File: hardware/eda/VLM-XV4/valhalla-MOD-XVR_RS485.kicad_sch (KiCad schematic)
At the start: 22 parts, among them J1 ModBUS, J2 BUS, U1 MAX3483, U2 ISO1410, U3 74LS06, U4 L78L33_TO92

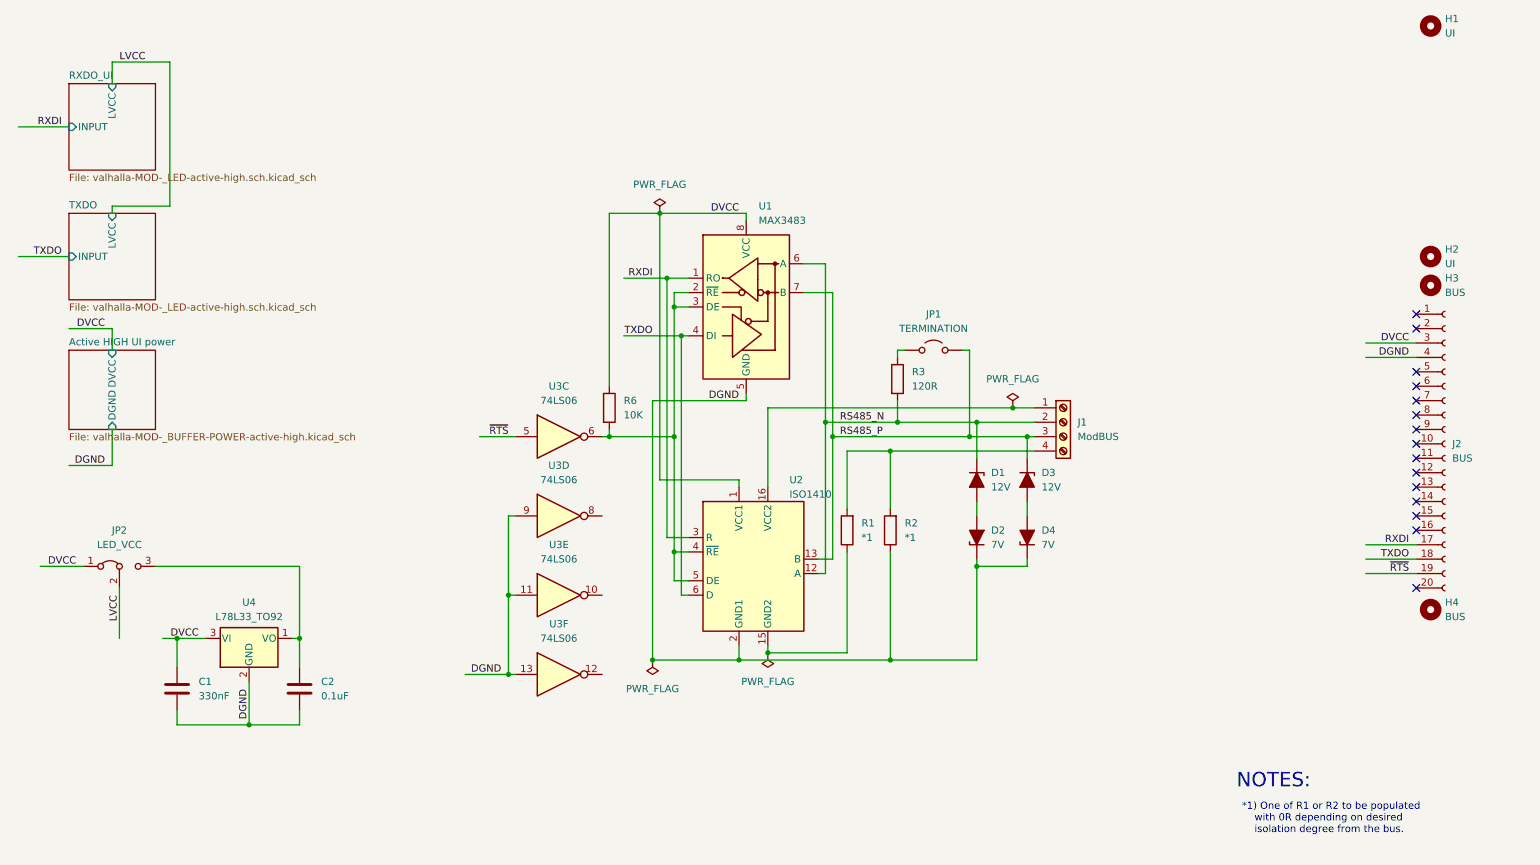
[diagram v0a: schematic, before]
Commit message: UPDATE: finalized schematic of XVR(RS485)
  - found a solution for Vio transparency using a buck-boost regulator
    module, this in turn opened the way to cheap 5V-powered RS485
    transceivers.
  - done initial component placement on the PCB, routing to follow.
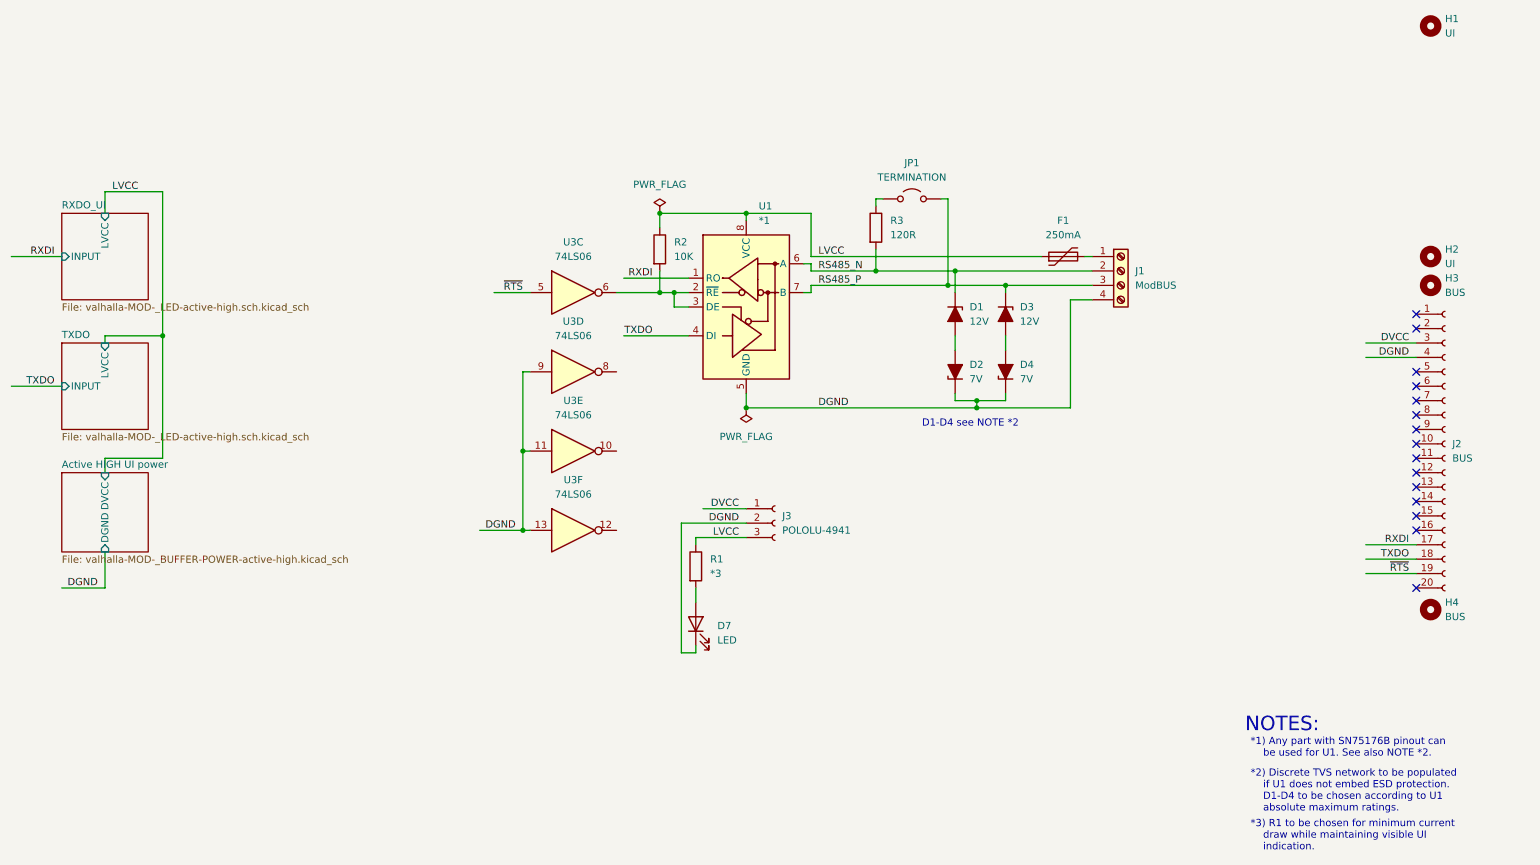
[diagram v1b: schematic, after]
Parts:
- removed C1: 330nF, Capacitor_THT:C_Rect_L4.6mm_W2.0mm_P2.50mm_MKS02_FKP02, symbol Device:C
- removed C2: 0.1uF, Capacitor_THT:C_Rect_L4.6mm_W2.0mm_P2.50mm_MKS02_FKP02, symbol Device:C
- removed JP2: LED_VCC, Connector_PinHeader_2.54mm:PinHeader_1x03_P2.54mm_Vertical, symbol Jumper:Jumper_3_Bridged12
- removed R2: *1, Resistor_SMD:R_1206_3216Metric, symbol Device:R
- removed U2: ISO1410, Package_SO:SOIC-16W_7.5x10.3mm_P1.27mm, symbol valhalla-collected:ISO1410
- removed U4: L78L33_TO92, Package_TO_SOT_THT:TO-92_Wide, symbol Regulator_Linear:L78L33_TO92
- added D7: LED, LED_THT:LED_D3.0mm_Horizontal_O1.27mm_Z2.0mm, symbol Device:LED
- added F1: 250mA, Capacitor_THT:C_Disc_D7.5mm_W4.4mm_P5.00mm, symbol Device:Polyfuse
- added J3: POLOLU-4941, Connector_PinSocket_2.54mm:PinSocket_1x03_P2.54mm_Horizontal, symbol Connector:Conn_01x03_Socket
- D1, D2, D3, D4: footprint (none) -> Diode_THT:D_DO-41_SOD81_P10.16mm_Horizontal
- JP1: footprint (none) -> Connector_PinHeader_2.54mm:PinHeader_1x02_P2.54mm_Vertical
- R1: value *1 -> *3; footprint Resistor_SMD:R_1206_3216Metric -> Resistor_THT:R_Axial_DIN0207_L6.3mm_D2.5mm_P5.08mm_Vertical
- R2: renamed from R6; footprint (none) -> Resistor_THT:R_Axial_DIN0207_L6.3mm_D2.5mm_P5.08mm_Vertical
- R3: footprint (none) -> Resistor_THT:R_Axial_DIN0207_L6.3mm_D2.5mm_P5.08mm_Vertical
- U1: value MAX3483 -> *1; footprint Package_SO:SOIC-8_3.9x4.9mm_P1.27mm -> Package_DIP:DIP-8_W7.62mm
- U3: footprint (none) -> Package_DIP:DIP-14_W7.62mm
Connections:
- net DGND: now also J1.4 (Pin_4), D7.1 (K), J3.2 (Pin_2)
- net DVCC: now also J3.1 (Pin_1); no longer R2.1, U1.8 (VCC)
- net LVCC: now also R1.1, R2.1, U1.8 (VCC), F1.1, J3.3 (Pin_3)
- net at R1.2: now also D7.2 (A); no longer J1.4 (Pin_4)
- net at J1.1 (Pin_1): now also F1.2
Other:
- note added: "*1) Any part with SN75176B pinout can be used for U1. See also NOTE *2."
- note added: "*2) Discrete TVS network to be populated if U1 does not embed ESD protection. D1-D4 to be chosen according to U1 absolute maximum ratings."
- note added: "*3) R1 to be chosen for minimum current draw while maintaining visible UI indication."
- note added: "D1-D4 see NOTE *2"
- note removed: "*1) One of R1 or R2 to be populated with 0R depending on desired isolation degree from the bus."
- moved on the sheet: D1, D2, D3, D4, J1, JP1, R2, R3, U3C, U3D, U3E, U3F

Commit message: UPDATE: XVR(RS485) RTM and XVR(RS232) started
  - after the final cosmetic tweaks, XVR(RS485) has reached RTM status
  - started work on XVR(RS232), schematic is mostly done -- save for
    the UI.
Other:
- moved on the sheet: F1
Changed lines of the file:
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@@
 	(wire
 		(pts
-			(xy 163.83 58.42) (xy 204.47 58.42)
+			(xy 163.83 58.42) (xy 195.58 58.42)
 		)
 		(stroke
@@
 	(wire
 		(pts
-			(xy 212.09 58.42) (xy 213.36 58.42)
+			(xy 203.2 58.42) (xy 213.36 58.42)
 		)
 		(stroke
@@
 		(property "Netclass" "DCD_Power"
 			(at 140.3985 48.26 0)
+			(effects
+				(font
+					(size 1.27 1.27)
+					(italic yes)
+				)
+				(justify left)
+			)
+		)
+	)
+	(netclass_flag ""
+		(length 2.54)
+		(shape round)
+		(at 212.09 58.42 0)
+		(fields_autoplaced yes)
+		(effects
+			(font
+				(size 1.27 1.27)
+			)
+			(justify left bottom)
+		)
+		(property "Netclass" "DCD_Power"
+			(at 212.7885 55.88 0)
 			(effects
 				(font
@@
 	(symbol
 		(lib_id "Device:Polyfuse")
-		(at 208.28 58.42 90)
+		(at 199.39 58.42 90)
 		(unit 1)
 		(exclude_from_sim no)
@@
 		(fields_autoplaced yes)
 		(property "Reference" "F1"
-			(at 208.28 52.07 90)
+			(at 199.39 52.07 90)
 			(effects
 				(font
@@
 		)
 		(property "Value" "250mA"
-			(at 208.28 54.61 90)
+			(at 199.39 54.61 90)
 			(effects
 				(font
@@
 		)
 		(property "Footprint" "Capacitor_THT:C_Disc_D7.5mm_W4.4mm_P5.00mm"
-			(at 213.36 57.15 0)
+			(at 204.47 57.15 0)
 			(effects
 				(font
@@
 		)
 		(property "Datasheet" "~"
-			(at 208.28 58.42 0)
+			(at 199.39 58.42 0)
 			(effects
 				(font
@@
 		)
 		(property "Description" "Resettable fuse, polymeric positive temperature coefficient"
-			(at 208.28 58.42 0)
-			(effects
-				(font
+			(at 199.39 58.42 0)
+			(effects
+				(font

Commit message: UPDATE: updated MOD-XVR(RS485) to the latest specification.
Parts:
- removed D7: LED, LED_THT:LED_D3.0mm_Horizontal_O1.27mm_Z2.0mm, symbol Device:LED
- removed J3: POLOLU-4941, Connector_PinSocket_2.54mm:PinSocket_1x03_P2.54mm_Horizontal, symbol Connector:Conn_01x03_Socket
- removed R1: *3, Resistor_THT:R_Axial_DIN0207_L6.3mm_D2.5mm_P5.08mm_Vertical, symbol Device:R
- added D5, D6: R, LED_THT:LED_D3.0mm_Horizontal_O1.27mm_Z2.0mm, symbol Device:LED
- added R4, R5: *3, Resistor_THT:R_Axial_DIN0207_L6.3mm_D2.5mm_P5.08mm_Vertical, symbol Device:R
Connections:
- net DGND: now also J2.6 (Pin_6), U3.7 (GND)
- net DVCC: now also F1.1, R2.1, U1.8 (VCC), U3.14 (VCC)
- net LVCC: now also J2.16 (Pin_16), R4.1, R5.1; no longer F1.1, R2.1, U1.8 (VCC)
- net RXDI: now also U3.1
- net TXDO: now also U3.3
- new net: D5.1 (K), U3.2
- new net: D5.2 (A), R4.2
- new net: D6.1 (K), U3.4
- new net: D6.2 (A), R5.2
- no-connect marks 15 -> 16
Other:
- removed sheet Active HIGH UI power
- removed sheet RXDO_UI
- removed sheet TXDO
- note added: "*3) R to be chosen for minimum current draw while maintaining visible UI indication."
- note removed: "*3) R1 to be chosen for minimum current draw while maintaining visible UI indication."
- title: Valhalla MOD RS485 Transceiver -> Valhalla MOD-XVR(RS485)
- moved on the sheet: D1, D2, D3, D4, F1, H1, H2, H3, H4, J1, J2, JP1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
